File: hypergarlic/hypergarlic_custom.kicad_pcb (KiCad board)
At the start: 2 copper layers, 238.8 x 87.7 mm, 52 parts, among them J1 AudioJack4dpb, J2 AudioJack4dpb, SW10 SW_Push, SW11 SW_Push, SW11_r1 SW_Push, SW12 SW_Push, SW12_r1 SW_Push, SW13_r1 SW_Push, SW14 SW_Push, SW15 SW_Push, SW15_r1 SW_Push, SW16 SW_Push, SW16_r1 SW_Push, SW17 SW_Push, SW17_r1 SW_Push, SW18 SW_Push, SW18_r1 SW_Push, SW2 SW_Push, SW20 SW_Push, SW20_r1 SW_Push, SW21 SW_Push, SW21_r1 SW_Push, SW2_r1 SW_Push, SW3 SW_Push, SW3_r1 SW_Push, SW4 SW_Push, SW4_r1 SW_Push, SW5 SW_Push, SW5_r1 SW_Push, SW6 SW_Push, SW6_r1 SW_Push, SW7_r1 SW_Push, SW8 SW_Push, SW8_r1 SW_Push, SW9 SW_Push, SW9_r1 SW_Push, U1 ProMicro-kbd, U2 ProMicro-kbd

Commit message: Flip rear logo to align orientation with front
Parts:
- removed the REF** at (199.3, 95.1)
- removed the REF** at (69.6, 95.1)
- added REF**: silk_pg1232_bottom, silkscreens:pg1232_bottom, F.Cu at (199.5, 95.1)
- added REF**: silk_pg1232_bottom, silkscreens:pg1232_bottom, B.Cu at (69.9, 95.1)
- moved REF** 0.41 mm to (69.9, 95.1)
- moved REF** 0.26 mm to (199.5, 95.1), turned to 0 degrees

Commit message: Use pro micro pin labels for A.dux
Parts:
- removed the REF** at (199.5, 95.1)
- removed the REF** at (69.9, 95.1)
- added REF**: silk_pg1232_bottom, silkscreens:pg1232_bottom, F.Cu at (199.5, 95.0)
- added REF**: silk_pg1232_bottom, silkscreens:pg1232_bottom, B.Cu at (69.9, 95.0)
- moved REF** 0.13 mm to (199.5, 95.0)
- moved REF** 0.13 mm to (69.9, 95.0)

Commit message: No logo version of Architeuthis, move silkscreens to the back of hypergarlic
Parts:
- removed the REF** at (199.5, 95.0) (x2)
- removed the REF** at (69.9, 95.0)
- added REF**: silk_pg1232_footprint, silkscreens:pg1232_footprint, B.Cu at (199.5, 95.0)
- added REF**: silk_pg1232_bottom, silkscreens:pg1232_bottom, B.Cu at (81.4, 95.0)
- REF**: moved to B.Cu
- moved REF** 7.87 mm to (62.1, 95.0), turned to 180 degrees

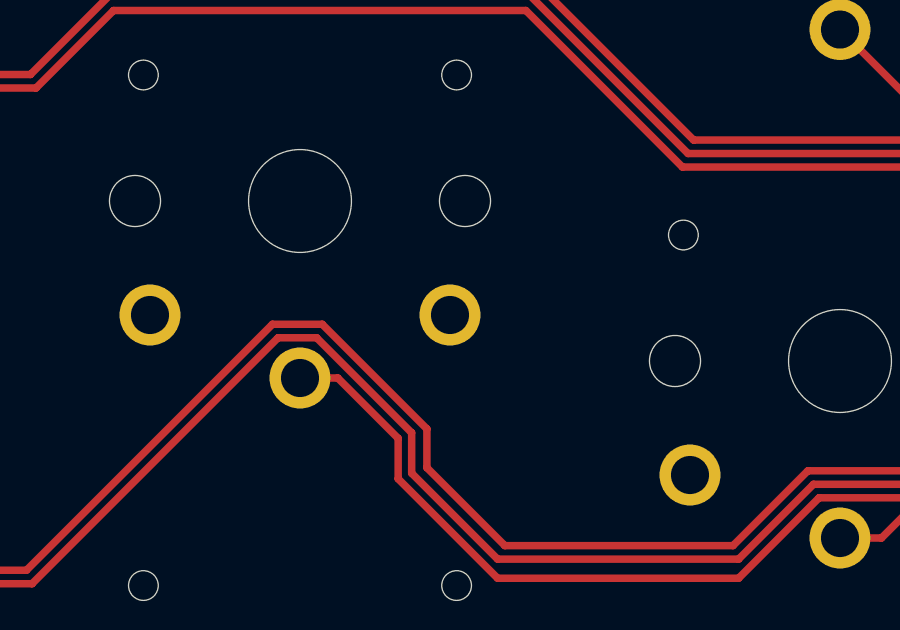
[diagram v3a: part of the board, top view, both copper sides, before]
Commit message: Corrected traces and removed extra switch drill holes
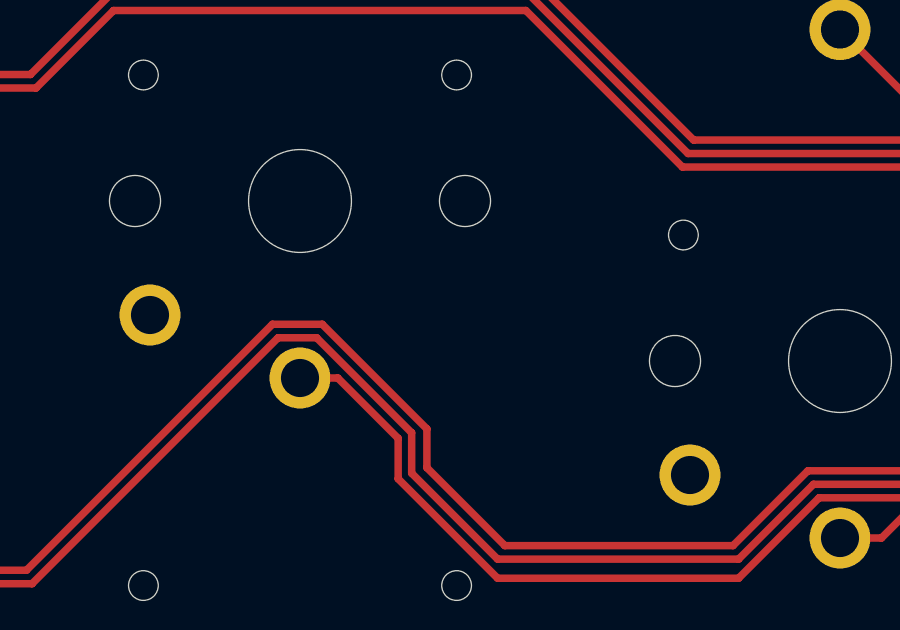
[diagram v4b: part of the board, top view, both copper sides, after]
